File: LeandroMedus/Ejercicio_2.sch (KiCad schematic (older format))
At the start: 0 parts

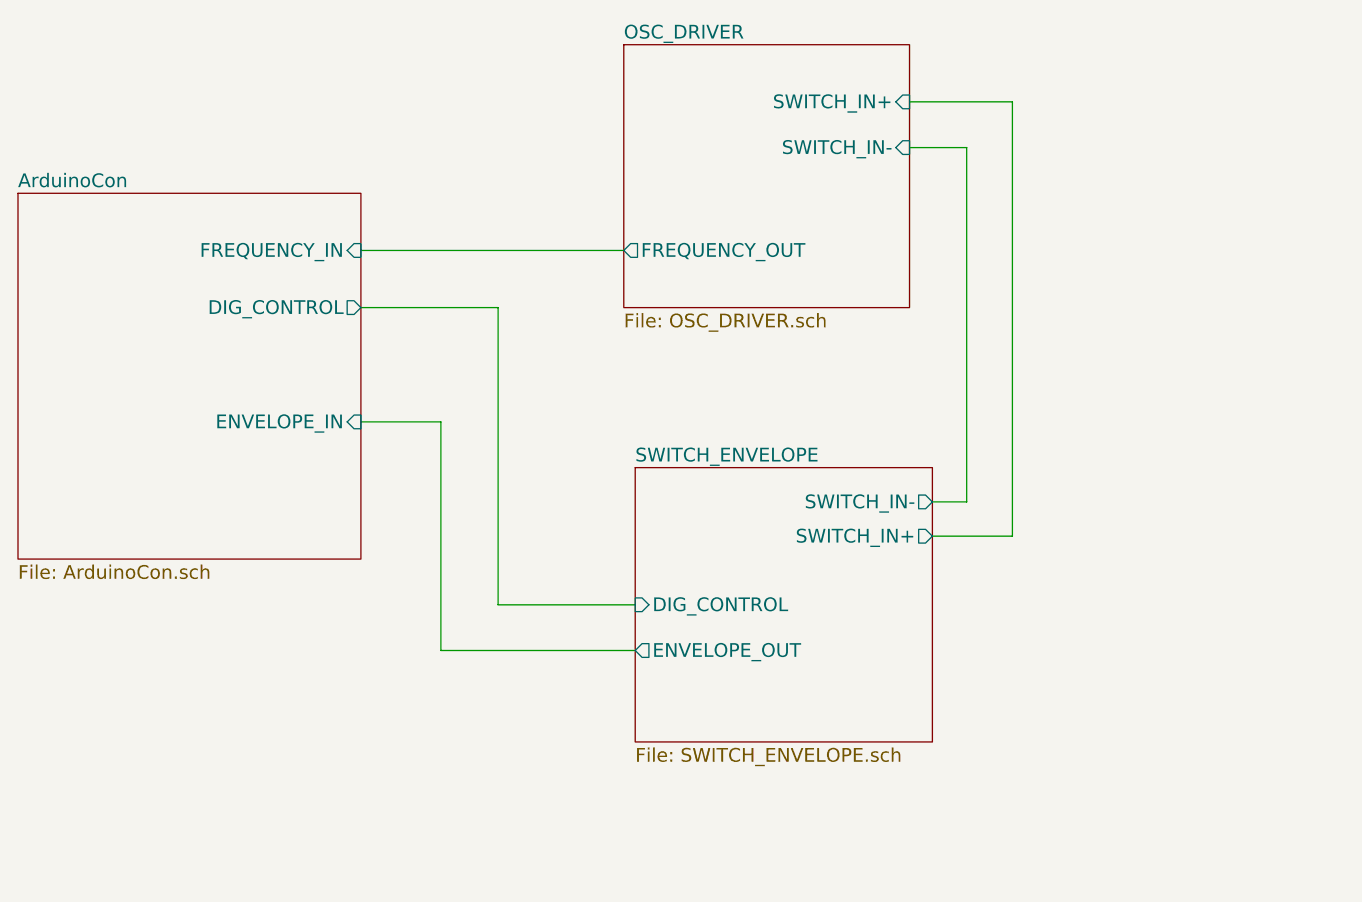
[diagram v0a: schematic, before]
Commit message: Fin clase 2 faltante
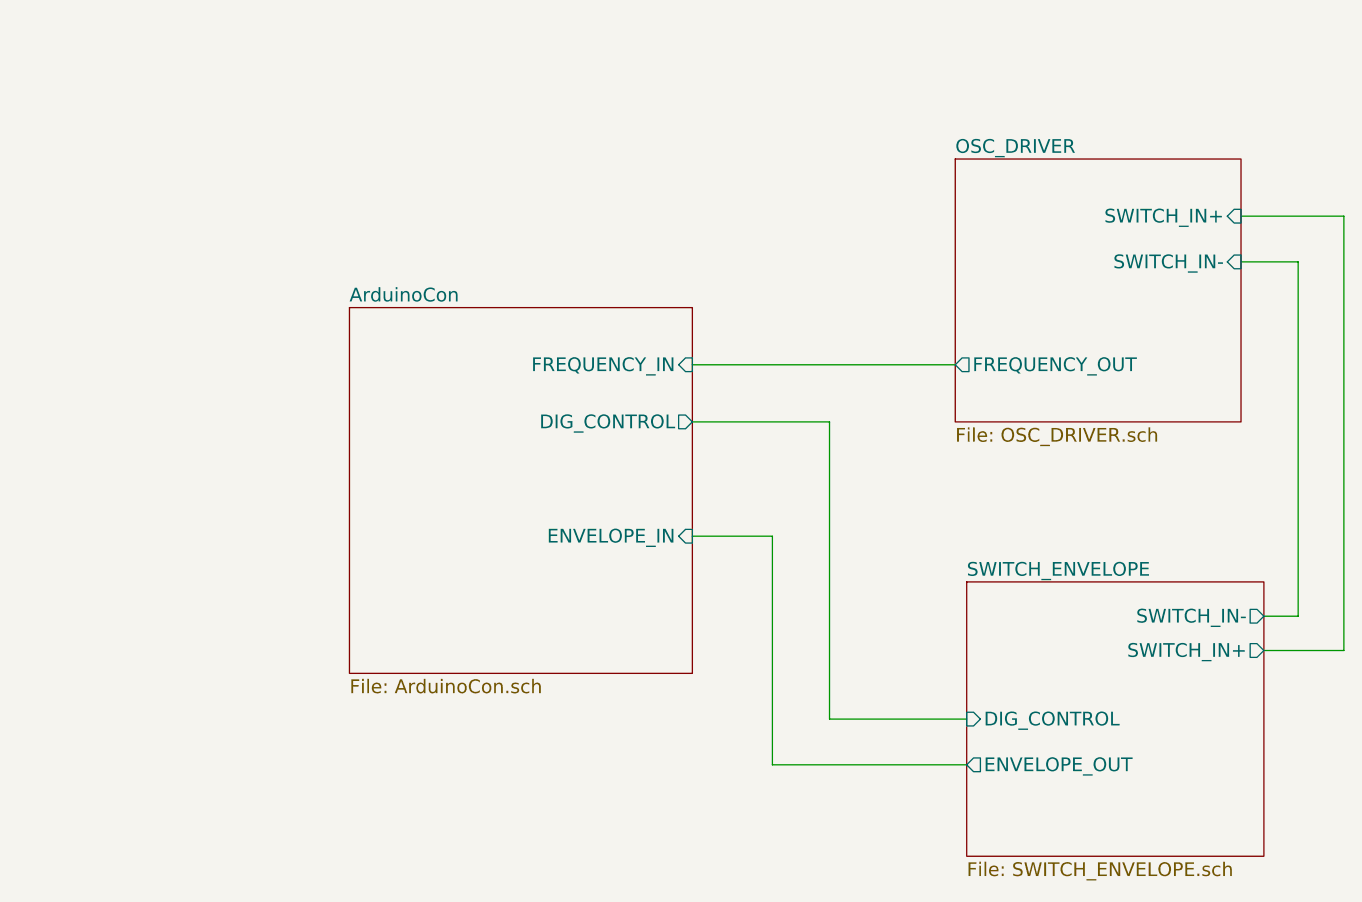
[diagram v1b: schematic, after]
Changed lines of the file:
@@
 $EndDescr
 $Sheet
-S 1750 2800 1500 1600
+S 3200 3300 1500 1600
 U 56F9338D
 F0 "ArduinoCon" 60
 F1 "ArduinoCon.sch" 60
-F2 "FREQUENCY_IN" I R 3250 3050 60
-F3 "DIG_CONTROL" O R 3250 3300 60
-F4 "ENVELOPE_IN" I R 3250 3800 60
+F2 "FREQUENCY_IN" I R 4700 3550 60
+F3 "DIG_CONTROL" O R 4700 3800 60
+F4 "ENVELOPE_IN" I R 4700 4300 60
 $EndSheet
 $Sheet
-S 4400 2150 1250 1150
+S 5850 2650 1250 1150
 U 56F933B1
 F0 "OSC_DRIVER" 60
 F1 "OSC_DRIVER.sch" 60
-F2 "FREQUENCY_OUT" O L 4400 3050 60
-F3 "SWITCH_IN+" I R 5650 2400 60
-F4 "SWITCH_IN-" I R 5650 2600 60
+F2 "FREQUENCY_OUT" O L 5850 3550 60
+F3 "SWITCH_IN+" I R 7100 2900 60
+F4 "SWITCH_IN-" I R 7100 3100 60
 $EndSheet
 $Sheet
-S 4450 4000 1300 1200
+S 5900 4500 1300 1200
 U 56F933C6
 F0 "SWITCH_ENVELOPE" 60
 F1 "SWITCH_ENVELOPE.sch" 60
-F2 "DIG_CONTROL" I L 4450 4600 60
-F3 "ENVELOPE_OUT" O L 4450 4800 60
-F4 "SWITCH_IN-" O R 5750 4150 60
-F5 "SWITCH_IN+" O R 5750 4300 60
+F2 "DIG_CONTROL" I L 5900 5100 60
+F3 "ENVELOPE_OUT" O L 5900 5300 60
+F4 "SWITCH_IN-" O R 7200 4650 60
+F5 "SWITCH_IN+" O R 7200 4800 60
 $EndSheet
 Wire Wire Line
-	3250 3050 4400 3050
+	4700 3550 5850 3550
 Wire Wire Line
-	3250 3300 3850 3300
+	4700 3800 5300 3800
 Wire Wire Line
-	3850 3300 3850 4600
+	5300 3800 5300 5100
 Wire Wire Line
-	3850 4600 4450 4600
+	5300 5100 5900 5100
 Wire Wire Line
-	3250 3800 3600 3800
+	4700 4300 5050 4300
 Wire Wire Line
-	3600 3800 3600 4800
+	5050 4300 5050 5300
 Wire Wire Line
-	3600 4800 4450 4800
+	5050 5300 5900 5300
 Wire Wire Line
-	5650 2600 5900 2600
+	7100 3100 7350 3100
 Wire Wire Line
-	5900 2600 5900 4150
+	7350 3100 7350 4650
 Wire Wire Line
-	5900 4150 5750 4150
+	7350 4650 7200 4650
 Wire Wire Line
-	5650 2400 6100 2400
+	7100 2900 7550 2900
 Wire Wire Line
-	6100 2400 6100 4300
+	7550 2900 7550 4800
 Wire Wire Line
-	6100 4300 5750 4300
+	7550 4800 7200 4800
 $EndSCHEMATC
